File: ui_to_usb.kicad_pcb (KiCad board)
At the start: 2 copper layers, 39.2 x 29 mm, 35 parts, among them J1 PM254-2-06-S-8.5, J2 TYPE-C-31-M-12, U1 FT232H, U2 93LCxxB, U3 USBLC6-2SC6, Y2 12M

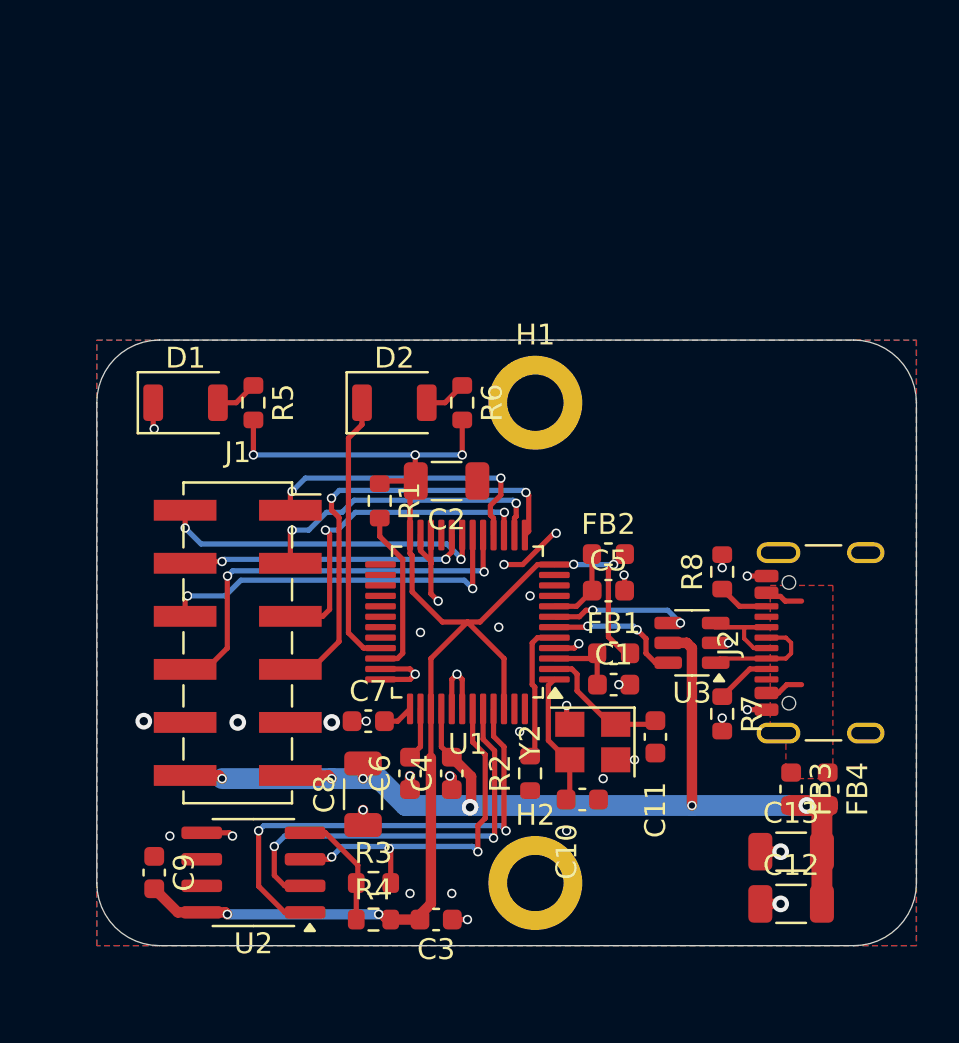
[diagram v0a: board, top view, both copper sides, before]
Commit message: add silkscreen
fix all DRC errors
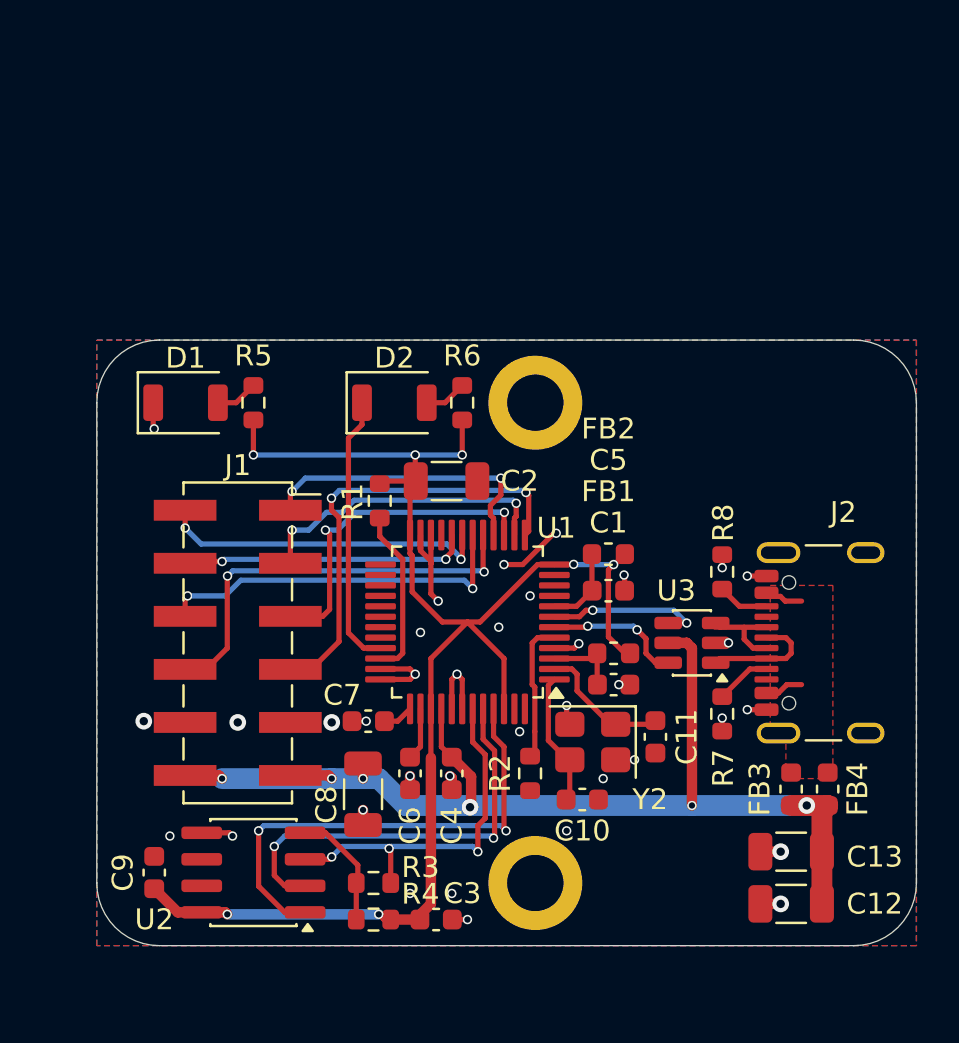
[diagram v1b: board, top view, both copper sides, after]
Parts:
- added G***: LOGO, LOGO, B.Cu at (85.2, 88.4)
- added G***: LOGO, LOGO, B.Cu at (92.3, 75.6)
- added G1: LOGO, LOGO, B.Cu at (94.5, 84.5)
- added G2: OSHW-Logo2_9.8x8mm_SilkScreen, Symbol:OSHW-Logo2_9.8x8mm_SilkScreen, B.Cu at (103.0, 83.2)
- added kibuzzard-6951B74E: G***, kibuzzard-6951B74E, B.Cu at (88.5, 71.1)
- added kibuzzard-6951B756: G***, kibuzzard-6951B756, B.Cu at (78.8, 71.1)
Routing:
- net Net-(J2-D+-PadA6): track 6.99 -> 9.52 mm
- net /D_P: track 7.01 -> 7.61 mm
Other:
- board text added: "Rev: - 12/2025"
- board text added: "https://github.com/betz-engineering/ui_to_usb"

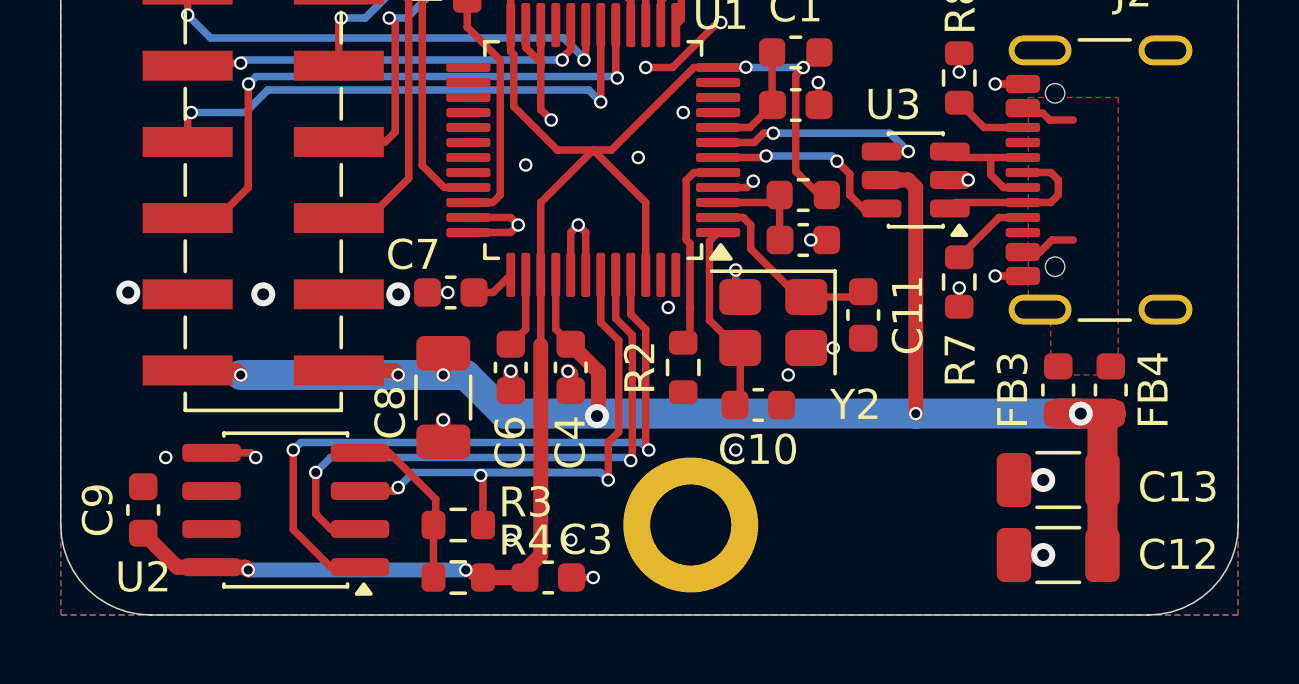
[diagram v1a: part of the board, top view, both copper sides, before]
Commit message: move flash chip out of the way
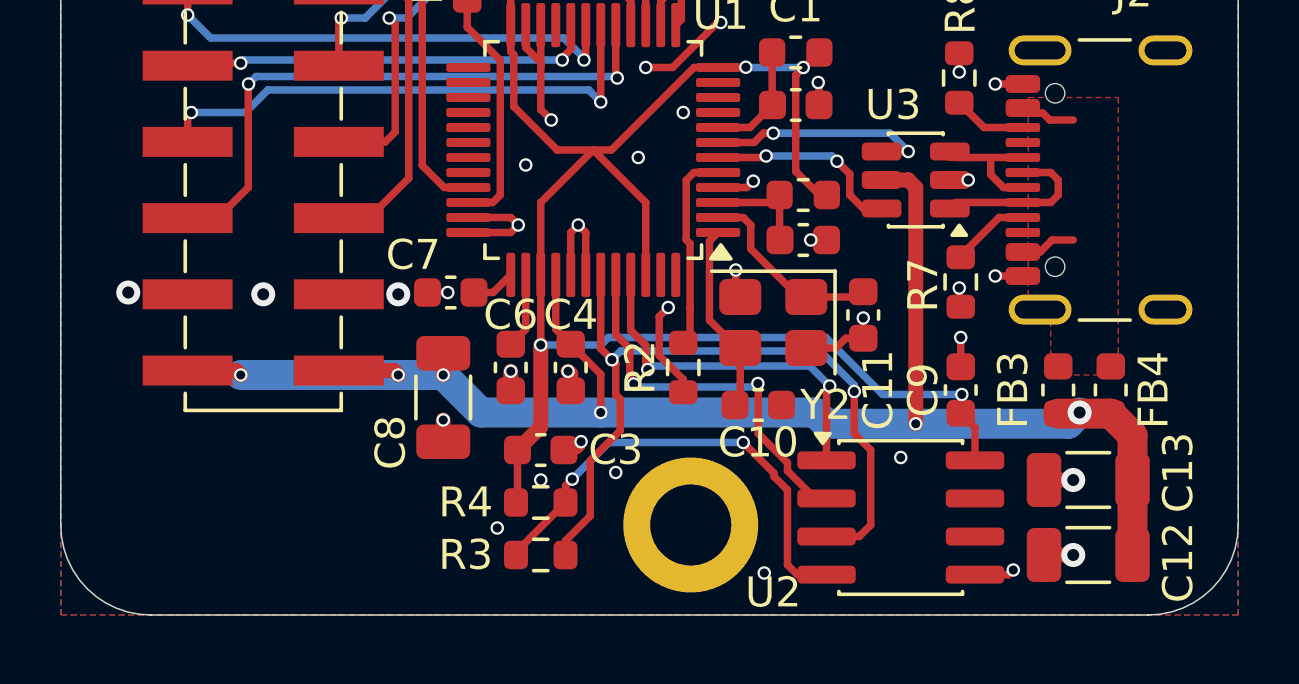
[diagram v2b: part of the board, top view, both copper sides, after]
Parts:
- removed kibuzzard-6951B74E: G***, kibuzzard-6951B74E
- removed kibuzzard-6951B756: G***, kibuzzard-6951B756
- added kibuzzard-6951C425: G***, kibuzzard-6951C425, B.Cu at (78.8, 71.1)
- added kibuzzard-6951C42C: G***, kibuzzard-6951C42C, B.Cu at (88.5, 71.1)
- moved C9 27.5 mm to (104.3, 87.0)
- moved U2 20.5 mm to (102.3, 91.3), turned to 0 degrees
- moved C3 4.26 mm to (90.3, 89.0)
- moved R4 3.72 mm to (90.3, 90.8), turned to 180 degrees
- moved R3 2.93 mm to (90.3, 92.5)
- moved C12 1.00 mm to (108.5, 92.5)
- moved C13 1.00 mm to (108.5, 90.0)
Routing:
- net /EECS: track 23.5 -> 12.3 mm
- net Net-(U2-DO): track 5.70 -> 15.6 mm, vias 0 -> 2
- net /EECLK: track 20.3 -> 13.1 mm
- net GND: track 31.4 -> 37.3 mm, vias 36 -> 37
- net Net-(U1-EEDATA): track 21.6 -> 25.6 mm, vias 3 -> 2
- net +3.3V: track 72.4 -> 74.3 mm
- net +5V: track 55.6 -> 56.3 mm

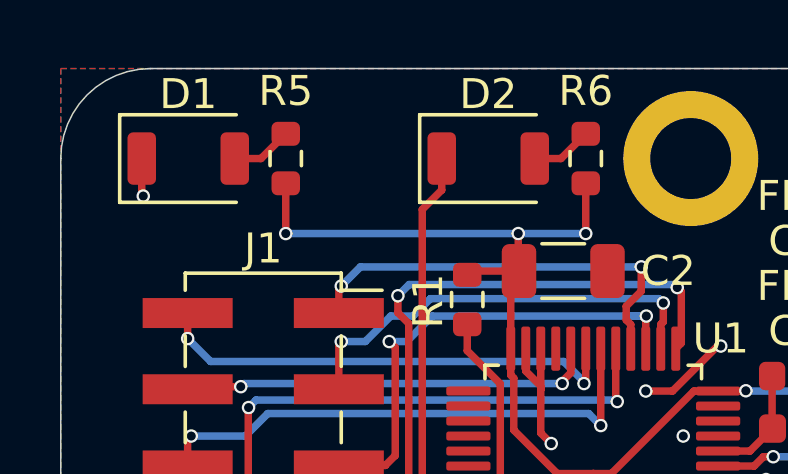
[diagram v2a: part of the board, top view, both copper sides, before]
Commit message: bigger cut-out for LEDs. Add README and renders
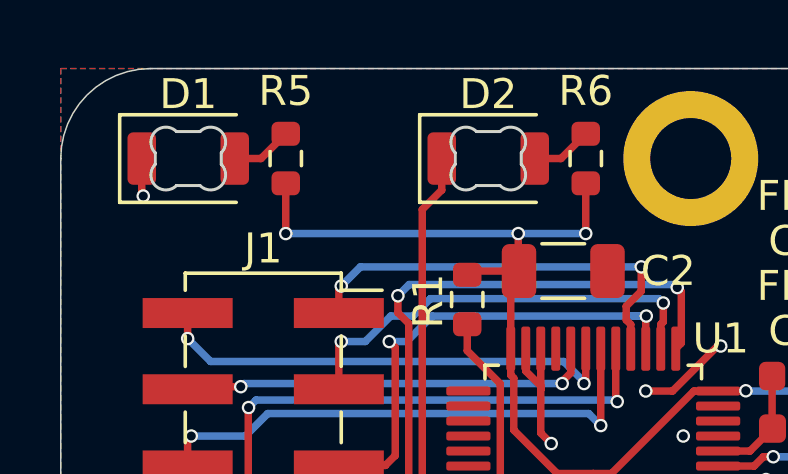
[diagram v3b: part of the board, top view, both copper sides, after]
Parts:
- D1, D2: footprint LED_SMD:LED_1206_3216Metric_ReverseMount_Hole1.8x2.4mm -> footprints:LED_1206_3216Metric_ReverseMount_Hole2.0x1.6mm

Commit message: check sch and pcb before production, looks ready
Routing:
- net GND: vias 37 -> 40
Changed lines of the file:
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@@
 			)
 			(rotate
-				(xyz -0 -180 -0)
+				(xyz -0 -180 -180)
 			)
 		)
@@
 			)
 			(rotate
-				(xyz 0 0 0)
+				(xyz -0 -0 -0)
 			)
 		)
@@
 			)
 			(rotate
-				(xyz -0 -180 -0)
+				(xyz -0 -180 -180)
 			)
 		)
@@
 	)
 	(via
+		(at 93.0052 71.0248)
+		(size 0.45)
+		(drill 0.3)
+		(layers "F.Cu" "B.Cu")
+		(free yes)
+		(net 2)
+	)
+	(via
 		(at 102.2552 89.2748)
 		(size 0.45)
@@
 	)
 	(via
+		(at 85.5052 70.2748)
+		(size 0.45)
+		(drill 0.3)
+		(layers "F.Cu" "B.Cu")
+		(free yes)
+		(net 2)
+	)
+	(via
 		(at 91.599927 88.746104)
 		(size 0.45)
@@
 	)
 	(via
+		(at 90.5052 70.2748)
+		(size 0.45)
+		(drill 0.3)
+		(layers "F.Cu" "B.Cu")
+		(free yes)
+		(net 2)
+	)
+	(via
 		(at 96.2552 74.7748)
 		(size 0.45)
@@
 	)
 	(segment
-		(start 79.250198 75.289798)
+		(start 90.6052 75.4248)
+		(end 90.5052 75.5248)
+		(width 0.25)
+		(layer "B.Cu")
+		(net 21)
+	)
+	(segment
+		(start 91.696217 76.0248)
+		(end 91.696217 75.965817)
+		(width 0.25)
+		(layer "B.Cu")
+		(net 21)
+	)
+	(segment
+		(start 79.4852 75.5248)
 		(end 78.4852 74.5248)
 		(width 0.25)
@@
 	)
 	(segment
-		(start 91.696217 75.965817)
-		(end 91.020198 75.289798)
+		(start 91.1552 75.4248)
+		(end 90.6052 75.4248)
 		(width 0.25)
 		(layer "B.Cu")
@@
 	)
 	(segment
-		(start 91.696217 76.0248)
-		(end 91.696217 75.965817)
+		(start 91.696217 75.965817)
+		(end 91.1552 75.4248)
 		(width 0.25)
 		(layer "B.Cu")
@@
 	)
 	(segment
-		(start 91.020198 75.289798)
-		(end 79.250198 75.289798)
+		(start 90.5052 75.5248)
+		(end 79.4852 75.5248)
 		(width 0.25)
 		(layer "B.Cu")
@@
 	)
 	(segment
+		(start 94.121496 86.808504)
+		(end 94.0052 86.9248)
+		(width 0.25)
+		(layer "B.Cu")
+		(net 32)
+	)
+	(segment
 		(start 93.3562 86.824327)
 		(end 93.456673 86.9248)
@@
 	)
 	(segment
-		(start 97.375874 86.9248)
-		(end 97.49217 86.808504)
+		(start 97.49217 86.808504)
+		(end 94.121496 86.808504)
 		(width 0.25)
 		(layer "B.Cu")
@@
 	(segment
 		(start 93.456673 86.9248)
-		(end 97.375874 86.9248)
+		(end 94.0052 86.9248)
 		(width 0.25)
 		(layer "B.Cu")

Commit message: improve BOM, ordered rev -
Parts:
- R5, R6: value 220R -> 1k5
- R7, R8: value 10k -> 5k1
- U2: value 93LCxxB -> 93LC56C
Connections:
- U2 pad 6: unconnected-(U2-NC-Pad6) -> +3.3V
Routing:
- net +3.3V: track 74.3 -> 79.2 mm
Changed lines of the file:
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@@
 	(net 43 "/D_P")
 	(net 44 "unconnected-(U2-NC-Pad7)")
-	(net 45 "unconnected-(U2-NC-Pad6)")
-	(net 46 "unconnected-(U1-ACBUS8-Pad32)")
+	(net 45 "unconnected-(U1-ACBUS8-Pad32)")
 	(footprint "Package_TO_SOT_SMD:SOT-23-6"
 		(layer "F.Cu")
@@
 			)
 		)
-		(property "Description" "BLM18AG601SN1D"
+		(property "Description" ""
 			(at 0 0 90)
 			(layer "F.Fab")
@@
 			)
 		)
+		(property "JLCPCB Part #" "C19330"
+			(at 0 0 270)
+			(unlocked yes)
+			(layer "F.Fab")
+			(hide yes)
+			(effects
+				(font
+					(size 1 1)
+					(thickness 0.15)
+				)
+			)
+		)
 		(property ki_fp_filters "Inductor_* L_* *Ferrite*")
 		(sheetname "/")
@@
 			)
 		)
-		(property "Value" "220R"
+		(property "Value" "1k5"
 			(at 0 1.43 90)
 			(layer "F.Fab")
@@
 			)
 		)
-		(property "Description" "BLM18AG601SN1D"
+		(property "Description" ""
 			(at 0 0 0)
 			(layer "F.Fab")
@@
 			)
 		)
+		(property "JLCPCB Part #" "C19330"
+			(at 0 0 0)
+			(unlocked yes)
+			(layer "F.Fab")
+			(hide yes)
+			(effects
+				(font
+					(size 1 1)
+					(thickness 0.15)
+				)
+			)
+		)
 		(property ki_fp_filters "Inductor_* L_* *Ferrite*")
 		(sheetname "/")
@@
 			)
 		)
-		(property "Value" "220R"
+		(property "Value" "1k5"
 			(at 0 1.43 90)
 			(layer "F.Fab")
@@
 			(layers "F.Cu" "F.Mask" "F.Paste")
 			(roundrect_rratio 0.25)
-			(net 46 "unconnected-(U1-ACBUS8-Pad32)")
+			(net 45 "unconnected-(U1-ACBUS8-Pad32)")
 			(pinfunction "ACBUS8")
 			(pintype "bidirectional+no_connect")
@@
 			)
 		)
-		(property "Description" "BLM18AG601SN1D"
+		(property "Description" ""
 			(at 0 0 0)
 			(layer "F.Fab")
@@
 			)
 		)
+		(property "JLCPCB Part #" "C19330"
+			(at 0 0 0)
+			(unlocked yes)
+			(layer "F.Fab")
+			(hide yes)
+			(effects
+				(font
+					(size 1 1)
+					(thickness 0.15)
+				)
+			)
+		)
 		(property ki_fp_filters "Inductor_* L_* *Ferrite*")
 		(sheetname "/")
@@
 			)
 		)
-		(property "Value" "93LCxxB"
+		(property "Value" "93LC56C"
 			(at 0 3.4 0)
 			(layer "F.Fab")
@@
 			)
 		)
-		(property "Description" "Serial EEPROM, 93 Series, 2.5V, DIP-8/SOIC-8"
+		(property "Description" "Serial EEPROM, 93 Series, with ORG Pin, 2.5V, DIP-8/SOIC-8"
 			(at 0 0 0)
 			(layer "F.Fab")
@@
 			(layers "F.Cu" "F.Mask" "F.Paste")
 			(roundrect_rratio 0.25)
-			(net 45 "unconnected-(U2-NC-Pad6)")
-			(pinfunction "NC")
-			(pintype "no_connect")
+			(net 3 "+3.3V")
+			(pinfunction "ORG")
+			(pintype "input")
 		)
 		(pad "7" smd roundrect
@@
 			)
 		)
-		(property "Value" "10k"
+		(property "Value" "5k1"
 			(at 0 1.43 90)
 			(layer "F.Fab")
@@
 			)
 		)
-		(property "Value" "10k"
+		(property "Value" "5k1"
 			(at 0 1.43 90)
 			(layer "F.Fab")
@@
 			)
 		)
+		(property "JLCPCB Part #" "C9002"
+			(at 0 0 180)
+			(unlocked yes)
+			(layer "F.Fab")
+			(hide yes)
+			(effects
+				(font
+					(size 1 1)
+					(thickness 0.15)
+				)
+			)
+		)
 		(property ki_fp_filters "Crystal*")
 		(sheetname "/")
@@
 			)
 		)
-		(property "Description" "BLM18AG601SN1D"
+		(property "Description" ""
 			(at 0 0 90)
 			(layer "F.Fab")
@@
 			)
 		)
+		(property "JLCPCB Part #" "C19330"
+			(at 0 0 270)
+			(unlocked yes)
+			(layer "F.Fab")
+			(hide yes)
+			(effects
+				(font
+					(size 1 1)
+					(thickness 0.15)
+				)
+			)
+		)
 		(property ki_fp_filters "Inductor_* L_* *Ferrite*")
 		(sheetname "/")
@@
 	)
 	(segment
+		(start 103.4292 89.6008)
+		(end 103.4292 91.6988)
+		(width 0.25)
+		(layer "F.Cu")
+		(net 3)
+	)
+	(segment
 		(start 99.5427 80.5248)
 		(end 99.7927 80.5248)
@@
 	)
 	(segment
+		(start 104.7302 89.3698)
+		(end 103.6602 89.3698)
+		(width 0.25)
+		(layer "F.Cu")
+		(net 3)
+	)
+	(segment
 		(start 89.5052 71.0248)
 		(end 89.5052 72.2498)
@@
 	)
 	(segment
+		(start 103.6602 89.3698)
+		(end 103.4292 89.6008)
+		(width 0.25)
+		(layer "F.Cu")
+		(net 3)
+	)
+	(segment
 		(start 90.2552 85.5248)
 		(end 90.2552 88.2498)
@@
 	)
 	(segment
+		(start 103.4292 91.6988)
+		(end 103.6402 91.9098)
+		(width 0.25)
+		(layer "F.Cu")
+		(net 3)
+	)
+	(segment
 		(start 90.2552 83.1873)
 		(end 90.2552 80.7748)
@@
 		(width 0.25)
 		(layer "F.Cu")
+		(net 3)
+	)
+	(segment
+		(start 103.6402 91.9098)
+		(end 104.7302 91.9098)
+		(width 0.25)
+		(layer "F.Cu")
